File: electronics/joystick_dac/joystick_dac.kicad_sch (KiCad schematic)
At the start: 3 parts, among them J1 Power/Signal Out, J2 Magnetometer

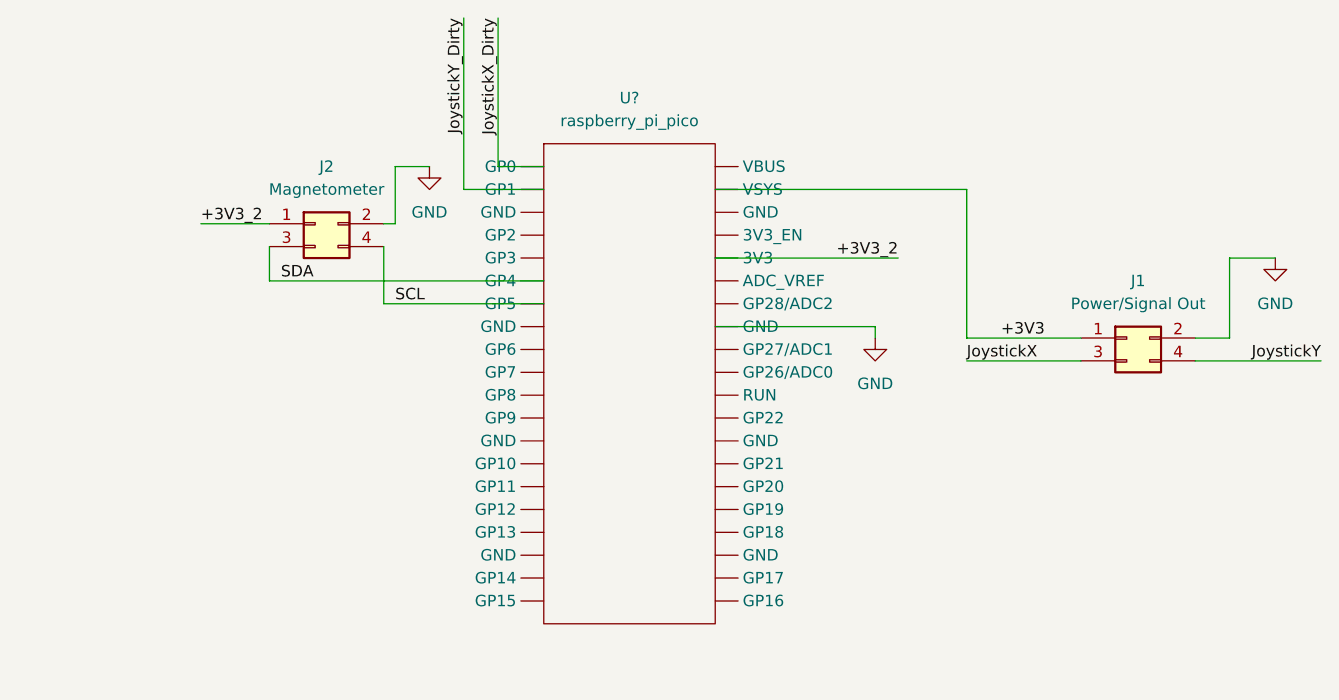
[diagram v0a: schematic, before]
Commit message: quick prototype of dac board for joystick
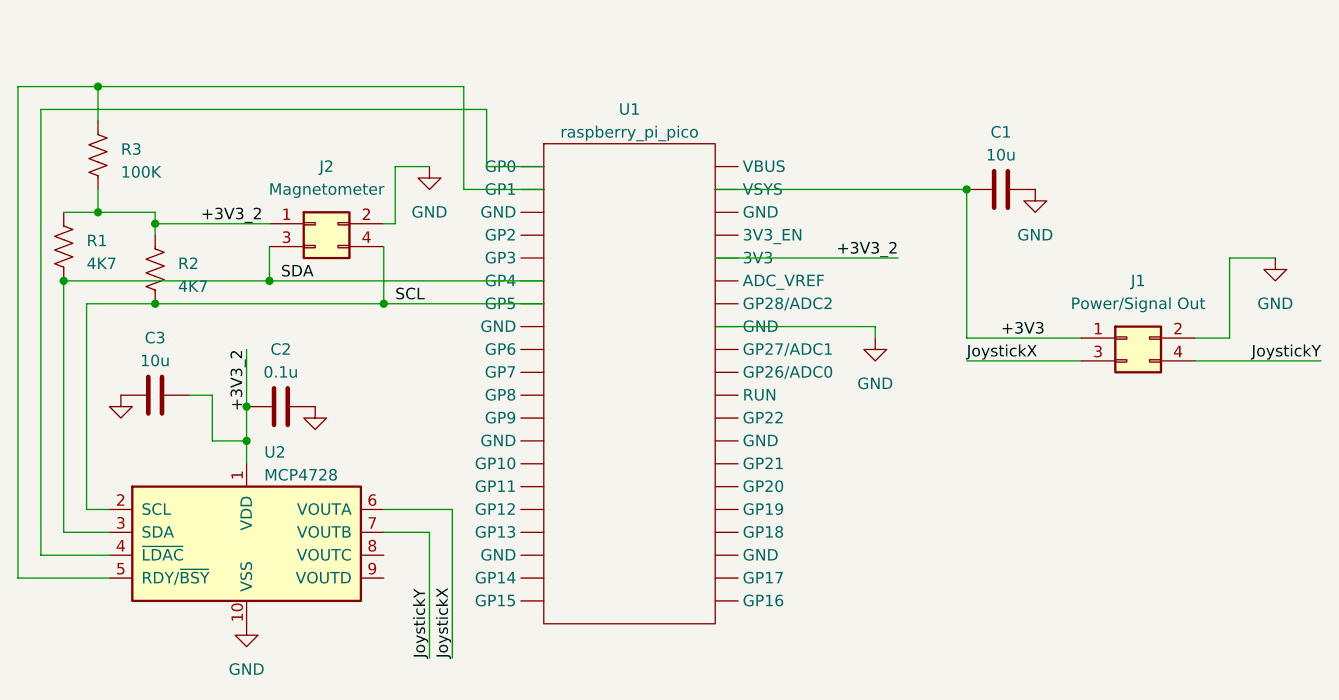
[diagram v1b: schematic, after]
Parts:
- added C1, C3: 10u, Capacitor_SMD:C_0603_1608Metric_Pad1.08x0.95mm_HandSolder, symbol Device:C
- added C2: 0.1u, Capacitor_SMD:C_0402_1005Metric_Pad0.74x0.62mm_HandSolder, symbol Device:C
- added R1, R2: 4K7, Resistor_THT:R_Axial_DIN0207_L6.3mm_D2.5mm_P10.16mm_Horizontal, symbol Device:R_US
- added R3: 100K, Resistor_THT:R_Axial_DIN0207_L6.3mm_D2.5mm_P10.16mm_Horizontal, symbol Device:R_US
- added U2: MCP4728, Package_SO:MSOP-10_3x3mm_P0.5mm, symbol Analog_DAC:MCP4728
- J1, J2: footprint (none) -> Connector_Molex:Molex_Mini-Fit_Jr_5569-04A2_2x02_P4.20mm_Horizontal
- U1: renamed from U?; footprint (none) -> custom_parts:raspberry_pi_pico
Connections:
- net +3V3: now also C1.1
- net +3V3_2: now also C2.1, C3.2, R1.1, R2.1, R3.2, U2.1 (VDD)
- net GND: now also C1.2, C2.2, C3.1, U2.10 (VSS)
- net JoystickX: now also U2.6 (VOUTA)
- net JoystickY: now also U2.7 (VOUTB)
- net SCL: now also R2.2, U2.2 (SCL)
- net SDA: now also R1.2, U2.3 (SDA)
- net JoystickX_Dirty: no longer names the net of U1.1 (GP0)
- net JoystickX_Dirty: now also U2.4 (~{LDAC})
- net JoystickY_Dirty: no longer names the net of U1.2 (GP1)
- net JoystickY_Dirty: now also R3.1, U2.5 (RDY/~{BSY})
